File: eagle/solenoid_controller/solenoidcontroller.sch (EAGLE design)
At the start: 44 parts, among them J1 ARDUINO_R3_SHIELD, Q1 PMV45EN, Q2 PMV45EN, Q3 PMV45EN, Q4 PMV45EN, Q5 PMV45EN, Q6 PMV45EN

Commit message: Cleaned up Baker's already A-OK board. Switched kickback components to bottom to minimimze copper length, fattened up power traces and reduced length, added text on top layer, re-numbered the solenoid terminals, stiched ground.
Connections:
- net N$15 renamed 6
- removed net N$13: J1.*D9, R2.1
- removed net N$14: J1.*D5, R1.1
- removed net N$16: J1.*D10, R9.1
- removed net N$17: J1.*D3, R7.1
- removed net N$18: J1.*D6, R8.1
- new net 1: J1.*D3, R1.1
- new net 2: J1.*D5, R2.1
- new net 3: J1.*D9, R9.1
- new net 4: J1.*D6, R7.1
- new net 5: J1.*D10, R8.1
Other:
- note added: "1"
- note added: "2"
- note added: "24V @ 2A external supply"
- note added: "3"
- note added: "4"
- note added: "5"
- note added: "6"
- note added: "Arduino Uno R3"
- note added: "RCS Solenoid Arduino Shield"
- moved on the sheet: C3, C6, D3, D6, J1, Q3, Q6, R12, R3, R6, R9, S3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

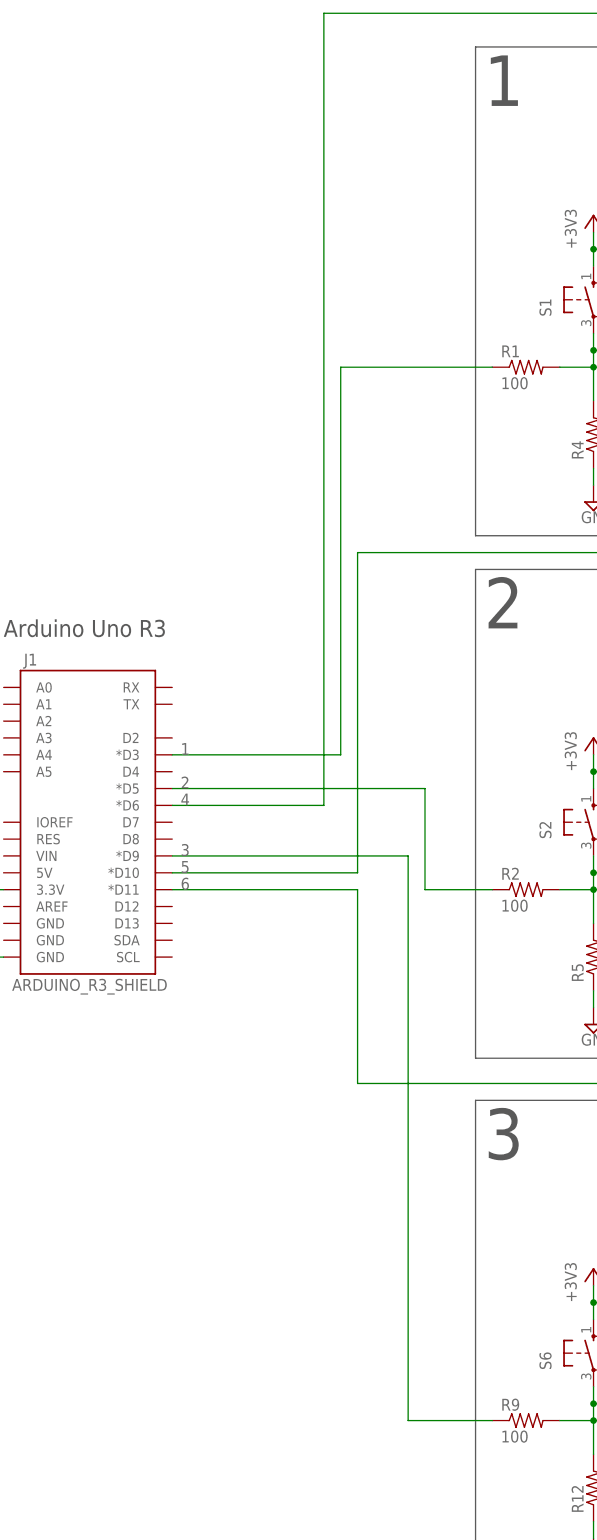
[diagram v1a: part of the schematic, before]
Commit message: Updated solenoid controller board; moved all SMD components to bottom layer and power traces to top layer.
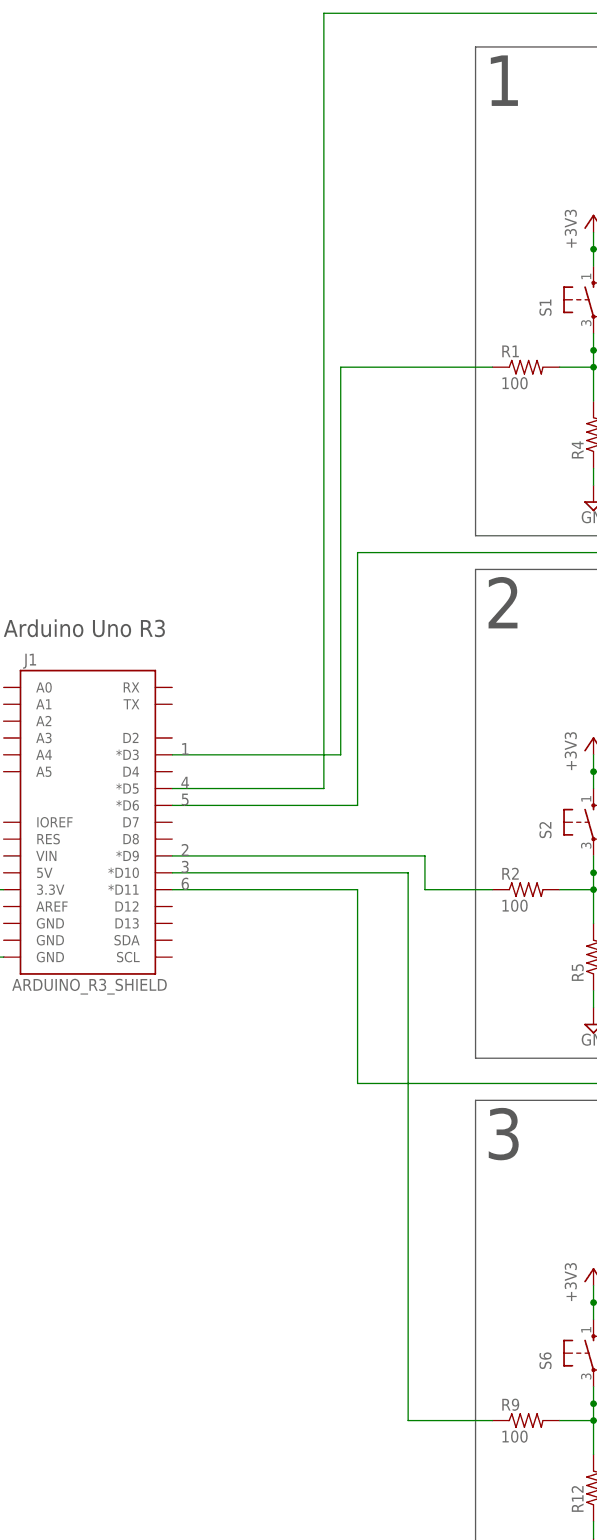
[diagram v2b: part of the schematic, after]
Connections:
- net 2: now also J1.*D9; no longer J1.*D5
- net 3: now also J1.*D10; no longer J1.*D9
- net 4: now also J1.*D5; no longer J1.*D6
- net 5: now also J1.*D6; no longer J1.*D10
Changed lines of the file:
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@@
 <?xml version="1.0" encoding="utf-8"?>
 <!DOCTYPE eagle SYSTEM "eagle.dtd">
-<eagle version="7.1.0">
+<eagle version="6.5.0">
 <drawing>
 <settings>
@@
 <setting verticaltext="up"/>
 </settings>
-<grid distance="0.05" unitdist="inch" unit="inch" style="lines" multiple="2" display="no" altdistance="0.01" altunitdist="inch" altunit="inch"/>
+<grid distance="0.1" unitdist="inch" unit="inch" style="lines" multiple="1" display="no" altdistance="0.01" altunitdist="inch" altunit="inch"/>
 <layers>
 <layer number="1" name="Top" color="4" fill="1" visible="no" active="no"/>
@@
 <pinref part="R9" gate="G$1" pin="1"/>
 <wire x1="132.08" y1="44.45" x2="119.38" y2="44.45" width="0.1524" layer="91"/>
-<wire x1="119.38" y1="44.45" x2="119.38" y2="129.54" width="0.1524" layer="91"/>
-<pinref part="J1" gate="G$1" pin="*D9"/>
-<wire x1="119.38" y1="129.54" x2="83.82" y2="129.54" width="0.1524" layer="91"/>
-<label x="85.09" y="129.54" size="1.778" layer="95"/>
+<wire x1="119.38" y1="44.45" x2="119.38" y2="127" width="0.1524" layer="91"/>
+<label x="85.09" y="127" size="1.778" layer="95"/>
+<pinref part="J1" gate="G$1" pin="*D10"/>
+<wire x1="83.82" y1="127" x2="119.38" y2="127" width="0.1524" layer="91"/>
 </segment>
 </net>
@@
 <pinref part="R2" gate="G$1" pin="1"/>
 <wire x1="132.08" y1="124.46" x2="121.92" y2="124.46" width="0.1524" layer="91"/>
-<pinref part="J1" gate="G$1" pin="*D5"/>
-<wire x1="83.82" y1="139.7" x2="121.92" y2="139.7" width="0.1524" layer="91"/>
-<wire x1="121.92" y1="139.7" x2="121.92" y2="124.46" width="0.1524" layer="91"/>
-<label x="85.09" y="139.7" size="1.778" layer="95"/>
+<label x="85.09" y="129.54" size="1.778" layer="95"/>
+<pinref part="J1" gate="G$1" pin="*D9"/>
+<wire x1="121.92" y1="129.54" x2="121.92" y2="124.46" width="0.1524" layer="91"/>
+<wire x1="121.92" y1="129.54" x2="83.82" y2="129.54" width="0.1524" layer="91"/>
 </segment>
 </net>
 <net name="4" class="0">
 <segment>
-<wire x1="106.68" y1="137.16" x2="106.68" y2="256.54" width="0.1524" layer="91"/>
+<wire x1="106.68" y1="139.7" x2="106.68" y2="256.54" width="0.1524" layer="91"/>
 <wire x1="106.68" y1="256.54" x2="205.74" y2="256.54" width="0.1524" layer="91"/>
 <wire x1="205.74" y1="256.54" x2="205.74" y2="203.2" width="0.1524" layer="91"/>
 <pinref part="R7" gate="G$1" pin="1"/>
 <wire x1="205.74" y1="203.2" x2="218.44" y2="203.2" width="0.1524" layer="91"/>
-<pinref part="J1" gate="G$1" pin="*D6"/>
-<wire x1="106.68" y1="137.16" x2="83.82" y2="137.16" width="0.1524" layer="91"/>
-<label x="85.09" y="137.16" size="1.778" layer="95"/>
+<label x="85.09" y="139.7" size="1.778" layer="95"/>
+<pinref part="J1" gate="G$1" pin="*D5"/>
+<wire x1="106.68" y1="139.7" x2="83.82" y2="139.7" width="0.1524" layer="91"/>
 </segment>
 </net>
@@
 <wire x1="205.74" y1="124.46" x2="205.74" y2="175.26" width="0.1524" layer="91"/>
 <wire x1="205.74" y1="175.26" x2="111.76" y2="175.26" width="0.1524" layer="91"/>
-<wire x1="111.76" y1="175.26" x2="111.76" y2="127" width="0.1524" layer="91"/>
-<pinref part="J1" gate="G$1" pin="*D10"/>
-<wire x1="83.82" y1="127" x2="111.76" y2="127" width="0.1524" layer="91"/>
-<label x="85.09" y="127" size="1.778" layer="95"/>
-</segment>
-</net>
+<wire x1="111.76" y1="175.26" x2="111.76" y2="137.16" width="0.1524" layer="91"/>
+<label x="85.09" y="137.16" size="1.778" layer="95"/>
+<pinref part="J1" gate="G$1" pin="*D6"/>
+<wire x1="83.82" y1="137.16" x2="111.76" y2="137.16" width="0.1524" layer="91"/>
+</segment>
+</net>
